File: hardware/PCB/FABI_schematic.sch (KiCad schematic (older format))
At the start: 27 parts, among them J1 Cliff_68125, J10 Conn_01x03_Male, J2 Cliff_68125, J3 Cliff_68125, J4 Cliff_68125, J5 Cliff_68125, J6 Cliff_68125, J7 Cliff_68125, J8 Cliff_68125, J9 Conn_02x05_Odd_Even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

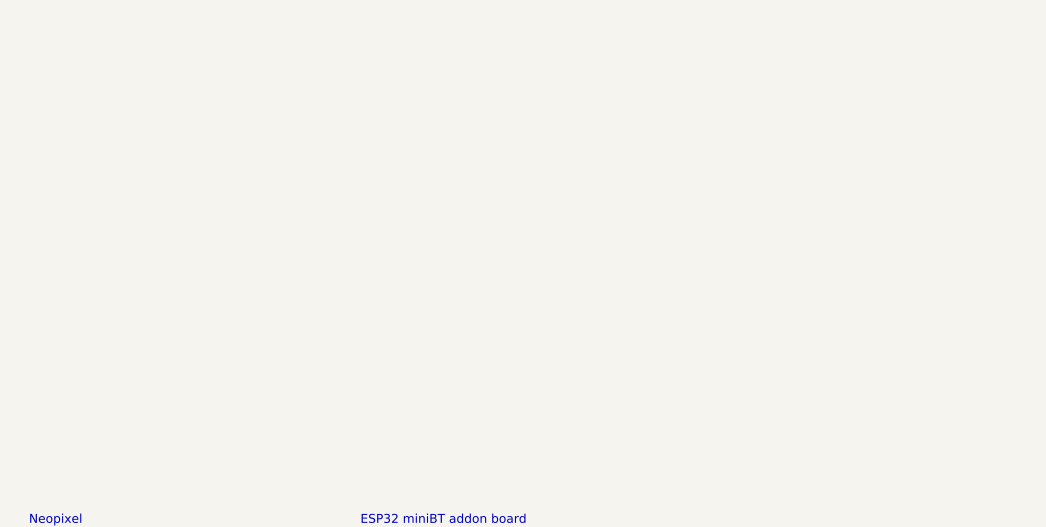
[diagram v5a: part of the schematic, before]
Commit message: +Display header & 3D design of display to find position Signed-off-by: fussthalerandreas <fussthaler.andreas1997@gmail.com>
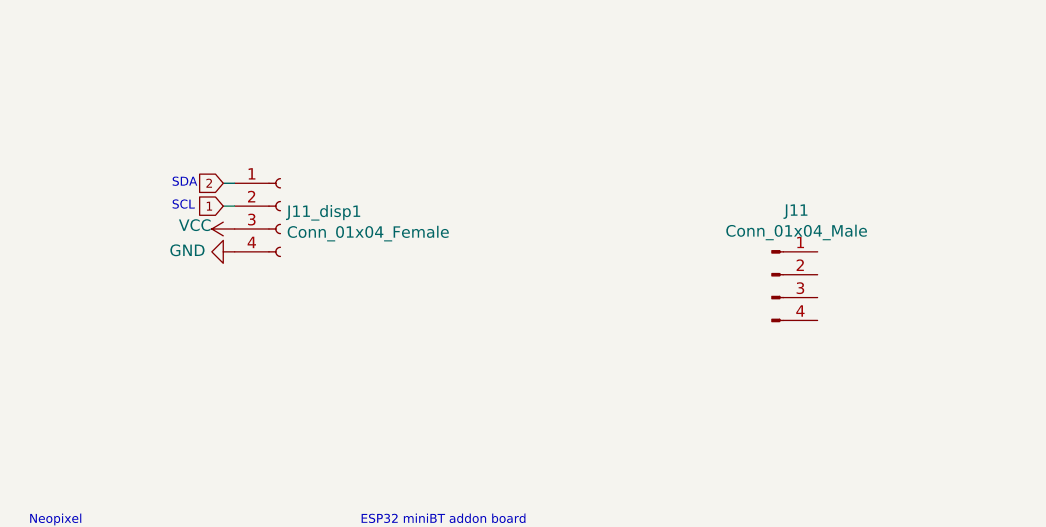
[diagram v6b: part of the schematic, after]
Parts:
- added J11: Conn_01x04_Male, Connector:display, symbol Connector:Conn_01x04_Male
- added J11_disp1: Conn_01x04_Female, Connector_PinSocket_2.54mm:PinSocket_1x04_P2.54mm_Vertical, symbol Connector:Conn_01x04_Female
- J9: footprint Connector_PinHeader_2.54mm:PinHeader_2x05_P2.54mm_Vertical -> Connector_PinSocket_2.54mm:PinSocket_2x05_P2.54mm_Vertical
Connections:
- net 1: now also J11_disp1.2 (Pin_2)
- net 2: now also J11_disp1.1 (Pin_1)
- net GND: now also J11_disp1.4 (Pin_4)
- net VCC: now also J11_disp1.3 (Pin_3)
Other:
- note added: "SCL"
- note added: "SDA"
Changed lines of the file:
@@
 F 0 "J9" H 7250 5467 50  0000 C CNN
 F 1 "Conn_02x05_Odd_Even" H 7250 5376 50  0000 C CNN
-F 2 "Connector_PinHeader_2.54mm:PinHeader_2x05_P2.54mm_Vertical" H 7200 5050 50  0001 C CNN
+F 2 "Connector_PinSocket_2.54mm:PinSocket_2x05_P2.54mm_Vertical" H 7200 5050 50  0001 C CNN
 F 3 "~" H 7200 5050 50  0001 C CNN
 	1    7200 5050
@@
 Wire Wire Line
 	2350 5850 2600 5850
+$Comp
+L power:VCC #PWR020
+U 1 1 602264EC
+P 6350 3050
+F 0 "#PWR020" H 6350 2900 50  0001 C CNN
+F 1 "VCC" V 6365 3223 50  0000 C CNN
+F 2 "" H 6350 3050 50  0001 C CNN
+F 3 "" H 6350 3050 50  0001 C CNN
+	1    6350 3050
+	0    -1   -1   0
+$EndComp
+Text GLabel 6300 2950 0    39   Input ~ 0
+1
+Text GLabel 6300 2850 0    39   Input ~ 0
+2
+Wire Wire Line
+	6300 2850 6350 2850
+Wire Wire Line
+	6300 2950 6350 2950
+$Comp
+L power:GND #PWR019
+U 1 1 6022BF5D
+P 6350 3150
+F 0 "#PWR019" H 6350 2900 50  0001 C CNN
+F 1 "GND" V 6355 3022 50  0000 R CNN
+F 2 "" H 6350 3150 50  0001 C CNN
+F 3 "" H 6350 3150 50  0001 C CNN
+	1    6350 3150
+	0    1    -1   0
+$EndComp
+$Comp
+L Connector:Conn_01x04_Female J11_disp1
+U 1 1 60220EC3
+P 6550 2950
+F 0 "J11_disp1" H 6578 2926 50  0000 L CNN
+F 1 "Conn_01x04_Female" H 6578 2835 50  0000 L CNN
+F 2 "Connector_PinSocket_2.54mm:PinSocket_1x04_P2.54mm_Vertical" H 6550 2950 50  0001 C CNN
+F 3 "~" H 6550 2950 50  0001 C CNN
+	1    6550 2950
+	1    0    0    -1
+$EndComp
+Text Notes 6075 2975 0    39   ~ 0
+SCL
+Text Notes 6075 2875 0    39   ~ 0
+SDA
+$Comp
+L Connector:Conn_01x04_Male J11
+U 1 1 60287AE3
+P 8700 3250
+F 0 "J11" H 8808 3531 50  0000 C CNN
+F 1 "Conn_01x04_Male" H 8808 3440 50  0000 C CNN
+F 2 "Connector:display" H 8700 3250 50  0001 C CNN
+F 3 "~" H 8700 3250 50  0001 C CNN
+	1    8700 3250
+	1    0    0    -1
+$EndComp
 $EndSCHEMATC

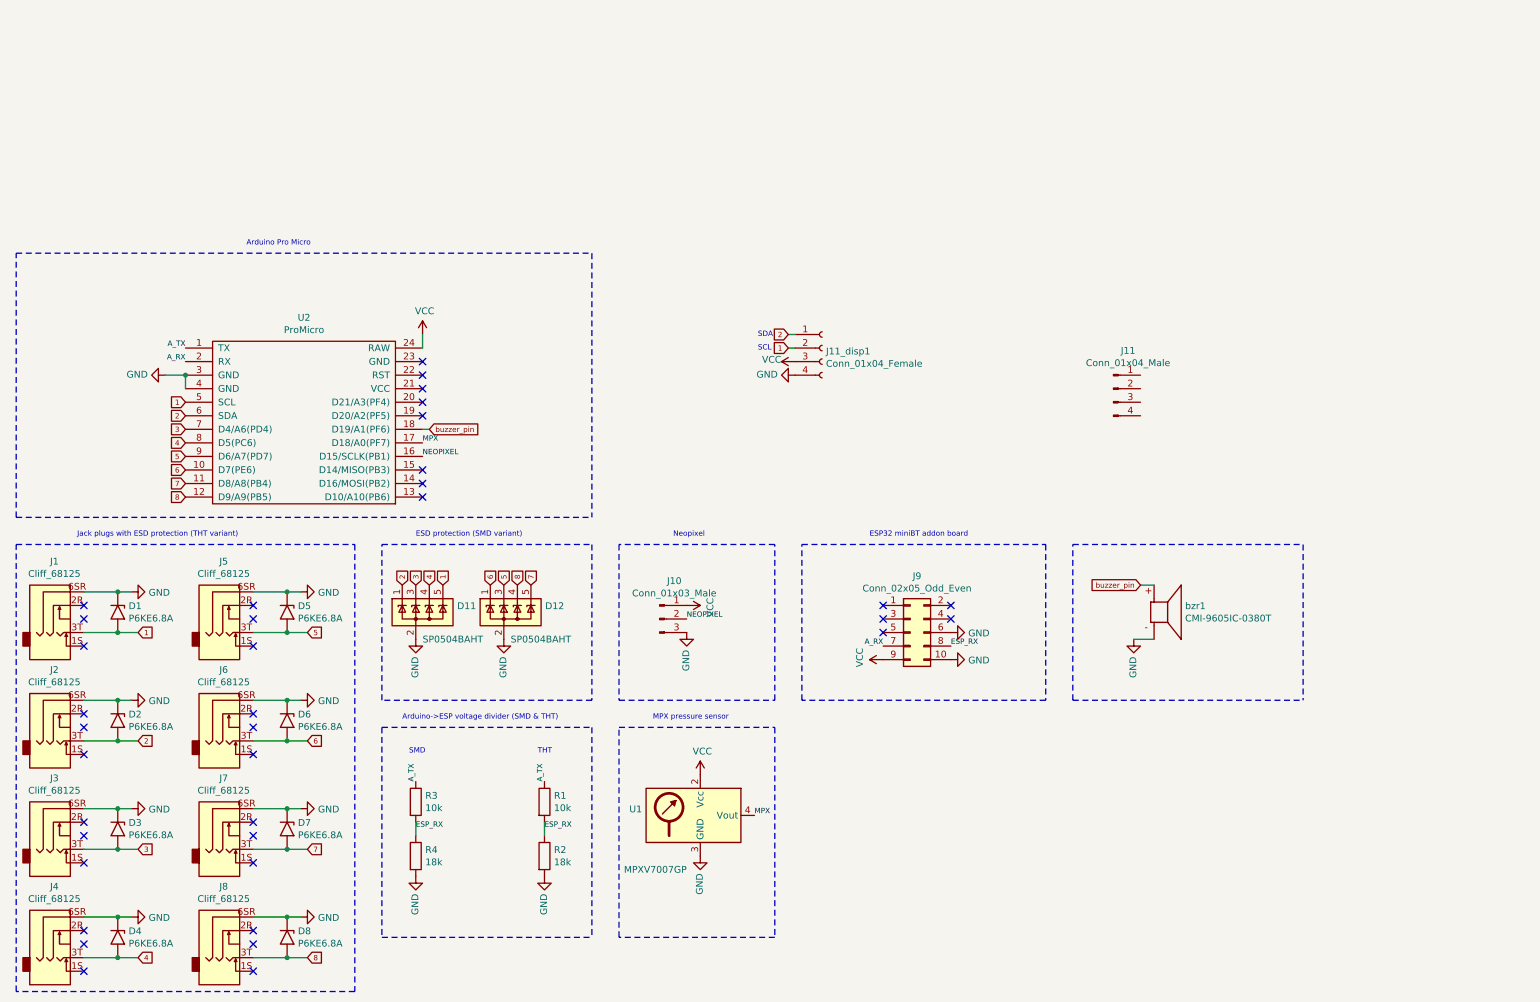
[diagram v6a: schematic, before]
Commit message: v2 of the PCB: added: Diplay connector, buzzer replaced: JackPlugs repositioned: JackPlugs, TVS, NeoPixel connector, pressure sensor
Signed-off-by: fussthalerandreas <fussthaler.andreas1997@gmail.com>
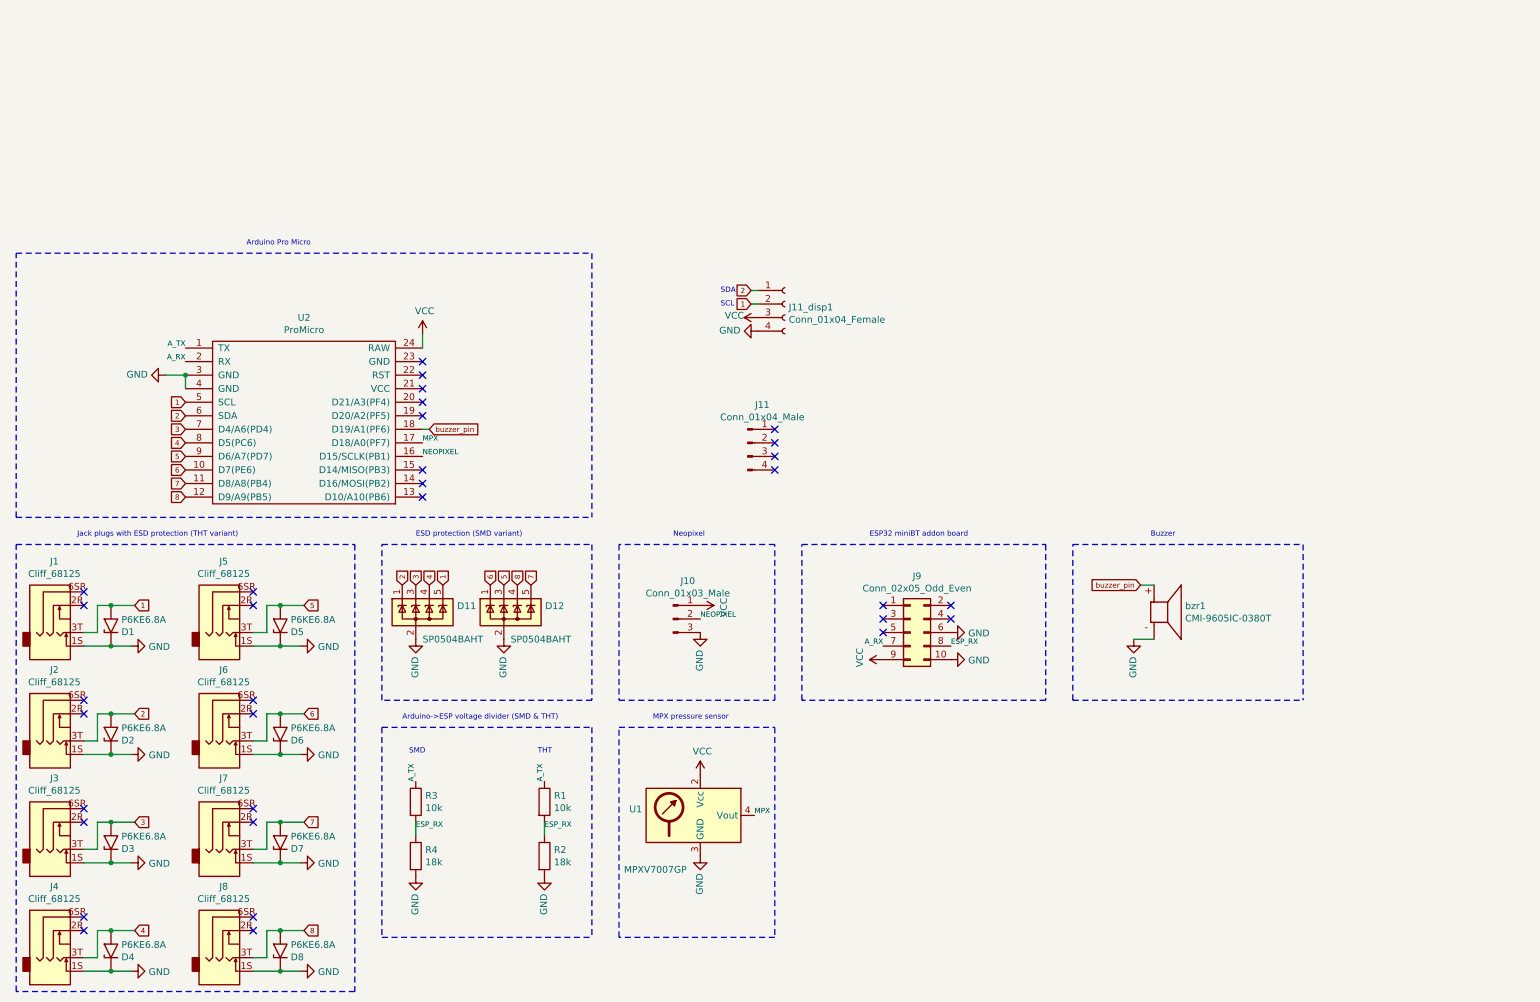
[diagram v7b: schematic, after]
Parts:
- D2, D3, D5, D6, D7, D8: Farnell (none) -> 1703028; RS-components (none) -> 171-9669
- D4: footprint Diode_THT:D_DO-201AD_P12.70mm_Horizontal -> Diode_THT:D_DO-201AE_P12.70mm_Horizontal; Farnell (none) -> 1703028; RS-components (none) -> 171-9669
- J9: footprint Connector_PinSocket_2.54mm:PinSocket_2x05_P2.54mm_Vertical -> Connector_PinHeader_2.54mm:PinHeader_2x05_P2.54mm_Vertical
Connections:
- net GND: now also J1.1S, J2.1S, J3.1S, J4.1S, J5.1S, J6.1S, J7.1S, J8.1S; no longer J1.6SR, J2.6SR, J3.6SR, J4.6SR, J5.6SR, J6.6SR, J7.6SR, J8.6SR
- no-connect marks 37 -> 33
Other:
- note added: "Buzzer"
- moved on the sheet: D1, J10, J11, J11_disp1

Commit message: SMD types of components added, TVS diode orientation, PullUps I2C Signed-off-by: fussthalerandreas <fussthaler.andreas1997@gmail.com>
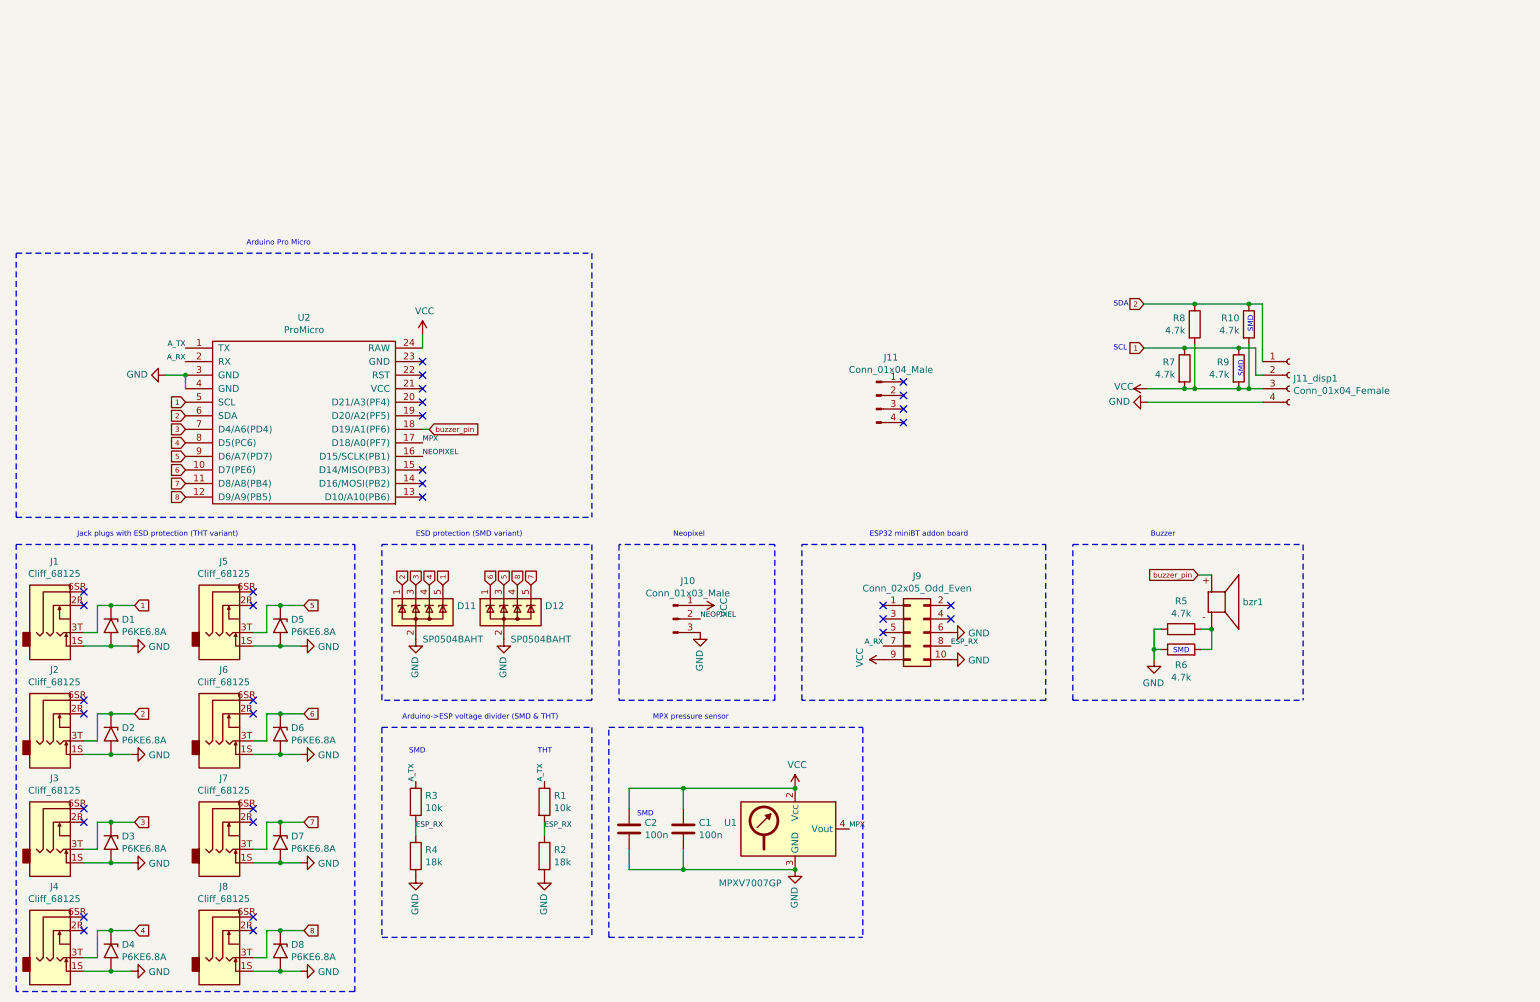
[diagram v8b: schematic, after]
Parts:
- added C1: 100n, Capacitor_THT:C_Disc_D5.0mm_W2.5mm_P5.00mm, symbol Device:C
- added C2: 100n, Capacitor_SMD:C_0805_2012Metric_Pad1.18x1.45mm_HandSolder, symbol Device:C
- added R10, R6, R9: 4.7k, Resistor_SMD:R_0805_2012Metric_Pad1.20x1.40mm_HandSolder, symbol Device:R
- added R5, R7, R8: 4.7k, Resistor_THT:R_Axial_DIN0204_L3.6mm_D1.6mm_P7.62mm_Horizontal, symbol Device:R
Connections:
- net 1: now also D1.1 (A1), R7.1, R9.1; no longer D1.2 (A2)
- net 2: now also D2.1 (A1), R10.1, R8.1; no longer D2.2 (A2)
- net 3: now also D3.1 (A1); no longer D3.2 (A2)
- net 4: now also D4.1 (A1); no longer D4.2 (A2)
- net 5: now also D5.1 (A1); no longer D5.2 (A2)
- net 6: now also D6.1 (A1); no longer D6.2 (A2)
- net 7: now also D7.1 (A1); no longer D7.2 (A2)
- net 8: now also D8.1 (A1); no longer D8.2 (A2)
- net GND: now also D1.2 (A2), D2.2 (A2), D3.2 (A2), D4.2 (A2), D5.2 (A2), D6.2 (A2), D7.2 (A2), D8.2 (A2), C1.2, C2.2, R5.1, R6.1; no longer D1.1 (A1), D2.1 (A1), D3.1 (A1), D4.1 (A1), D5.1 (A1), D6.1 (A1), D7.1 (A1), D8.1 (A1), bzr1.N
- net VCC: now also C1.1, C2.1, R10.2, R7.2, R8.2, R9.2
- new net: R5.2, R6.2, bzr1.N
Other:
- moved on the sheet: J11, U1, bzr1
